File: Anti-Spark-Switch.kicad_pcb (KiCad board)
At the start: 2 copper layers, 63.2 x 30 mm, 40 parts, among them P2 Pad_Conn, P5 Pad_Conn, P6 Pad_Conn, P7 CONN_01X04, Q1 IRFS7530, Q2 IRFS7530, Q3 IRFS7530

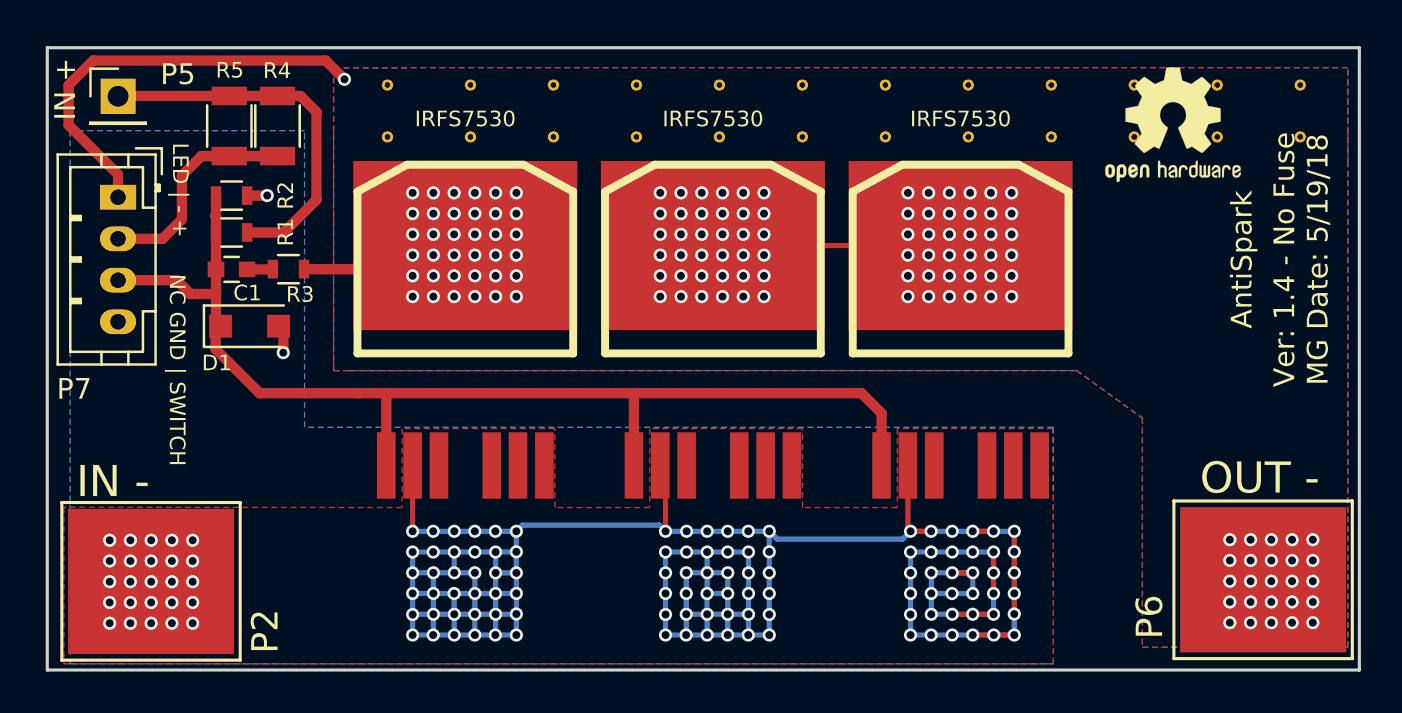
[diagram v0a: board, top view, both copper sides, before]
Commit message: change mosfet to BSC026N08NS5
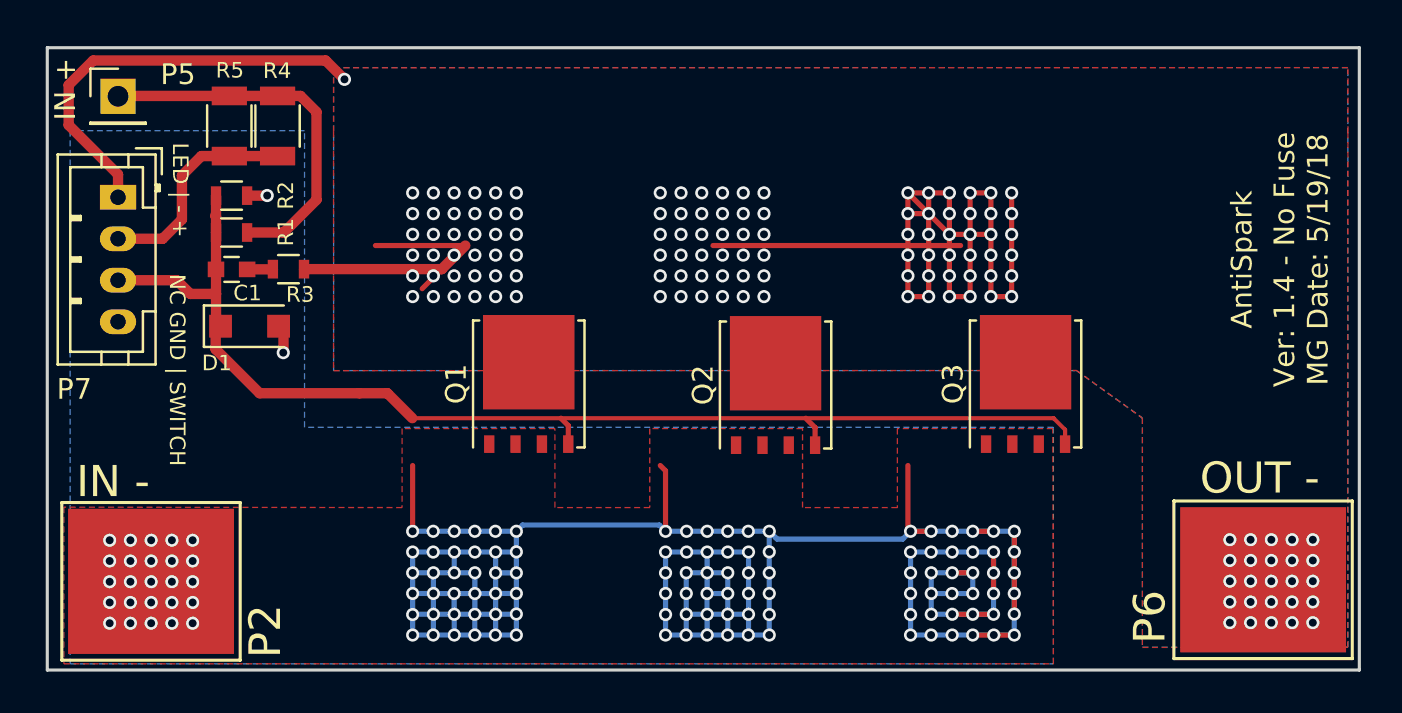
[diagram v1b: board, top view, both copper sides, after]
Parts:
- removed ? (x24): , Kinetic_Footprints:via-0.45mm
- removed G***: LOGO, w_logo:Logo_silk_high_voltage_10x8.5mm
- removed REF***: OSHW-Logo2_7.3x6mm_SilkScreen, Symbols:OSHW-Logo2_7.3x6mm_SilkScreen
- Q1, Q2, Q3: value IRFS7530 -> BSC026N08NS5; footprint sparkparts:D2PAK-7-GDS -> Package_TO_SOT_SMD:TDSON-8-1
- moved Q3 3.23 mm to (162.8, 105.0), turned to 90 degrees
- moved Q1 3.15 mm to (138.9, 105.0), turned to 90 degrees
- moved Q2 3.13 mm to (150.8, 105.0), turned to 90 degrees
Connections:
- P6 pad 1: Net-(P6-Pad1) -> Net-(P6-P1)
- P7 pad 1: Net-(P6-Pad1) -> Net-(P6-P1)
- R3 pad 1: Net-(P6-Pad1) -> Net-(P6-P1)
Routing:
- net Net-(P6-Pad1): track 116.3 -> 0.00 mm, vias 134 -> 0
- net Net-(P6-P1): track 0.00 -> 116.3 mm, vias 0 -> 134
- net /SW_NC: track 55.4 -> 58.7 mm
- added copper zone on B.Cu, net Net-(P6-P1)
- added copper zone on F.Cu, net Net-(P6-P1)
- removed copper zone on B.Cu, net Net-(P6-Pad1)
- removed copper zone on F.Cu, net Net-(P6-Pad1)
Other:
- net class Default removed
